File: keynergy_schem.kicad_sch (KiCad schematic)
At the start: 4 parts, among them SW1 SW_DPDT_x2, SW2 SW_DPDT_x2, SW3 SW_DPDT_x2, SW4 SW_DPDT_x2

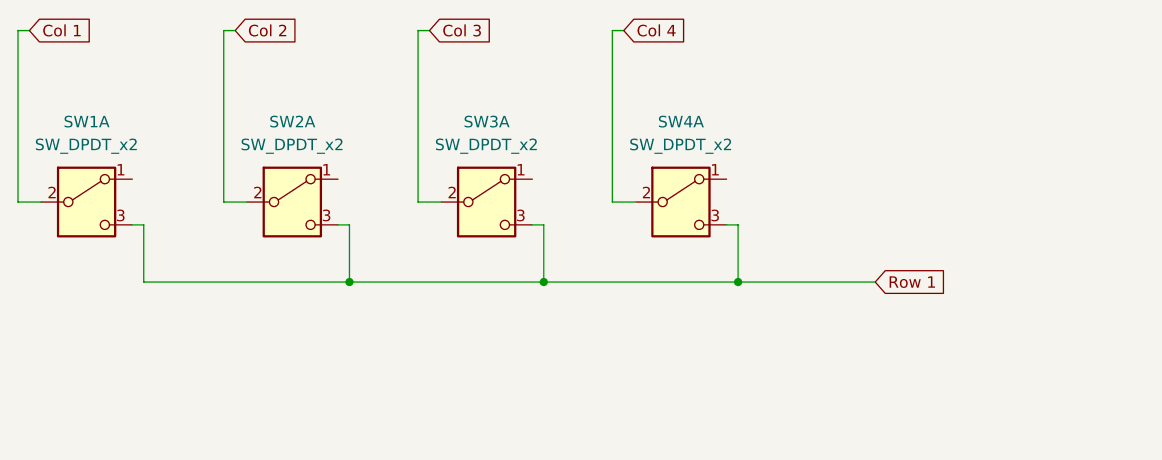
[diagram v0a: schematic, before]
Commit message: custom selonoid key added
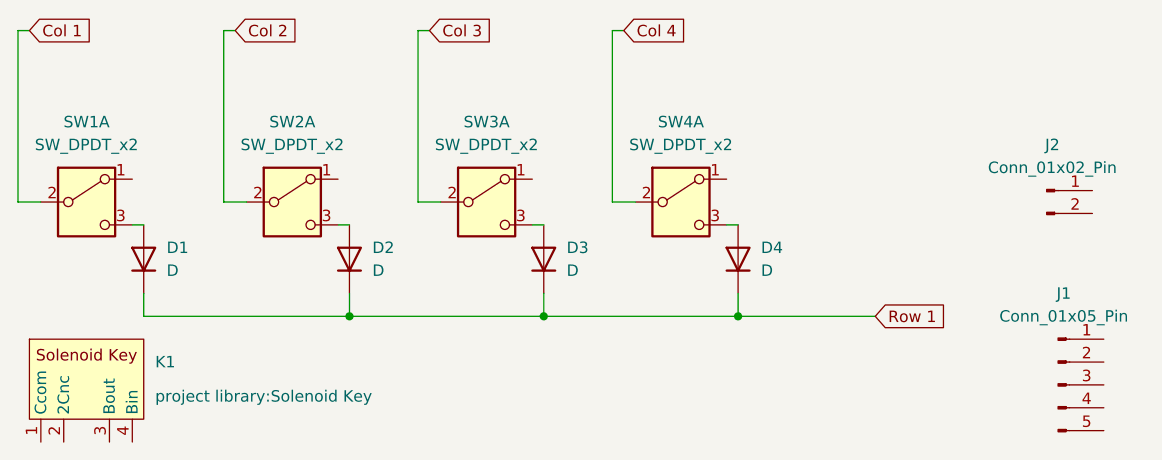
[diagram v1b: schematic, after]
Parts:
- added D1, D2, D3, D4: D, Diode_THT:D_DO-35_SOD27_P7.62mm_Horizontal, symbol Device:D
- added J1: Conn_01x05_Pin, symbol Connector:Conn_01x05_Pin
- added J2: Conn_01x02_Pin, symbol Connector:Conn_01x02_Pin
- added K1: ~, project library:Solenoid Key, symbol Key_symbol:Solenoid_Key
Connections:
- net Row 1: now also D1.1 (K), D2.1 (K), D3.1 (K), D4.1 (K); no longer SW1.3 (C), SW2.3 (C), SW3.3 (C), SW4.3 (C)
- new net: D1.2 (A), SW1.3 (C)
- new net: D3.2 (A), SW3.3 (C)
- new net: D2.2 (A), SW2.3 (C)
- new net: D4.2 (A), SW4.3 (C)

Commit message: new files
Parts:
- removed J1: Conn_01x05_Pin, symbol Connector:Conn_01x05_Pin
- removed J2: Conn_01x02_Pin, symbol Connector:Conn_01x02_Pin
- removed SW1, SW2, SW3, SW4: SW_DPDT_x2, symbol Switch:SW_DPDT_x2
- added J1: Conn_01x03_Pin, Connector_PinHeader_2.54mm:PinHeader_1x03_P2.54mm_Vertical, symbol Connector:Conn_01x03_Pin
- added J3: Conn_01x04_Pin, Connector_PinHeader_2.54mm:PinHeader_1x04_P2.54mm_Vertical, symbol Connector:Conn_01x04_Pin
- added K2, K3, K4: ~, project library:Solenoid Key, symbol Key_symbol:Solenoid_Key
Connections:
- net Col 1: now also K1.4 (Bin), J3.1 (Pin_1)
- net Col 2: now also J3.2 (Pin_2), K2.4 (Bin)
- net Col 3: now also J3.3 (Pin_3), K3.4 (Bin), K4.4 (Bin)
- net Col 4: now also J3.4 (Pin_4)
- net Row 1: now also J1.1 (Pin_1)
- net at D1.2 (A): now also K1.3 (Bout)
- net at D3.2 (A): now also K3.3 (Bout)
- net at D2.2 (A): now also K2.3 (Bout)
- net Row 3: now reaches K1.1 (C1)
- net Row 3: now also J1.3 (Pin_3)
- net at K1.2 (C2): now also K2.1 (C1)
- net at D4.2 (A): now also K4.3 (Bout)
- new net: K2.2 (C2), K3.1 (C1)
- new net: K3.2 (C2), K4.1 (C1)
- new net Row 2: J1.2 (Pin_2), K4.2 (C2)
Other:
- moved on the sheet: D1, D2, D3, D4, K1

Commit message: new files
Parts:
- added D10, D11, D5, D6, D7, D8, D9: D, Diode_THT:D_DO-35_SOD27_P7.62mm_Horizontal, symbol Device:D
- added J2, J6, J8: Conn_01x03_Pin, Connector_PinHeader_2.54mm:PinHeader_1x03_P2.54mm_Vertical, symbol Connector:Conn_01x03_Pin
- added J4, J5, J7: Conn_01x04_Pin, Connector_PinHeader_2.54mm:PinHeader_1x04_P2.54mm_Vertical, symbol Connector:Conn_01x04_Pin
- added K10, K11, K5, K6, K7, K8, K9: ~, project library:Solenoid Key, symbol Key_symbol:Solenoid_Key
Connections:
- net Row 2: now also D5.1 (K), D6.1 (K), D7.1 (K), J2.1 (Pin_1); no longer J1.2 (Pin_2), K4.2 (C2)
- net Col 1 renamed Col 1-1
- net Col 2 renamed Col 1-2
- net Col 3 renamed Col 1-3
- net Col 1-3: no longer K4.4 (Bin)
- net Col 4 renamed Col 1-4
- net Col 1-4: now also K4.4 (Bin)
- net Row 3 renamed Coil 1-2
- new net: D11.2 (A), K11.3 (Bout)
- new net: K6.2 (C2), K7.1 (C1)
- new net: D7.2 (A), K7.3 (Bout)
- new net: D10.2 (A), K10.3 (Bout)
- new net: K5.2 (C2), K6.1 (C1)
- new net: D6.2 (A), K6.3 (Bout)
- new net: D8.2 (A), K8.3 (Bout)
- new net: D5.2 (A), K5.3 (Bout)
- new net: K10.2 (C2), K11.1 (C1)
- new net: D9.2 (A), K9.3 (Bout)
- new net: K8.2 (C2), K9.1 (C1)
- new net Coil 1-1: J1.2 (Pin_2), K4.2 (C2)
- new net Coil 2-1: J2.2 (Pin_2), K7.2 (C2)
- new net Coil 2-2: J2.3 (Pin_3), K5.1 (C1)
- new net Coil 5-1: J6.2 (Pin_2), K9.2 (C2)
- new net Coil 5-2: J6.3 (Pin_3), K8.1 (C1)
- new net Coil 5-3: J8.2 (Pin_2), K11.2 (C2)
- new net Coil 5-4: J8.3 (Pin_3), K10.1 (C1)
- new net Col 2-1: J4.1 (Pin_1), K5.4 (Bin)
- new net Col 2-2: J4.2 (Pin_2), K6.4 (Bin)
- new net Col 2-3: J4.3 (Pin_3), K7.4 (Bin)
- new net Col 2-4: J4.4 (Pin_4)
- new net Col 5: D10.1 (K), D11.1 (K), J8.1 (Pin_1)
- new net Col 5-1: J5.1 (Pin_1), K8.4 (Bin)
- new net Col 5-2: J5.2 (Pin_2), K9.4 (Bin)
- new net Col 5-3: J5.3 (Pin_3)
- new net Col 5-4: J5.4 (Pin_4)
- new net Row 5: D8.1 (K), D9.1 (K), J6.1 (Pin_1)
- new net Row 5-1: J7.1 (Pin_1), K10.4 (Bin)
- new net Row 5-2: J7.2 (Pin_2), K11.4 (Bin)
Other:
- moved on the sheet: D1, D2, D3, D4, J1, J3, K1, K2, K3, K4

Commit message: new
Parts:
- removed J4: Conn_01x04_Pin, Connector_PinHeader_2.54mm:PinHeader_1x04_P2.54mm_Vertical, symbol Connector:Conn_01x04_Pin
- added J4: Conn_01x03_Pin, Connector_PinHeader_2.54mm:PinHeader_1x03_P2.54mm_Vertical, symbol Connector:Conn_01x03_Pin
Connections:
- net Col 2-1: now also J4.1 (Pin_1)
- net Col 2-2: now also J4.2 (Pin_2)
- net Col 2-3: now also J4.3 (Pin_3)
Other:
- note added: "Row 1, Col 1-4"
- note added: "Row 2-4, Col 1-3"
- note added: "Row 2/3 - 4/5, Col 5"
- note added: "Row 5, Col 1-2/3"
- moved on the sheet: J7, J8

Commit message: new update
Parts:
- removed J5, J7: Conn_01x04_Pin, Connector_PinHeader_2.54mm:PinHeader_1x04_P2.54mm_Vertical, symbol Connector:Conn_01x04_Pin
- added J5, J7: Conn_01x02_Pin, Connector_PinHeader_2.54mm:PinHeader_1x02_P2.54mm_Vertical, symbol Connector:Conn_01x02_Pin
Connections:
- net Col 5-1: now also J5.1 (Pin_1)
- net Col 5-2: now also J5.2 (Pin_2)
- net Row 5-1: now also J7.1 (Pin_1)
- net Row 5-2: now also J7.2 (Pin_2)
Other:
- note added: "Row 5, Col 1/2-3"
- note removed: "Row 5, Col 1-2/3"

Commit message: new
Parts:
- added A2: RaspberryPi_Pico_W, Module:RaspberryPi_Pico_Common_THT, symbol MCU_Module:RaspberryPi_Pico_W
- added BT1: Battery_Cell, symbol Device:Battery_Cell
- added C1: 1000uF, Capacitor_THT:CP_Radial_D8.0mm_P5.00mm, symbol Device:C_Polarized
- added D12, D13, D15: D, Diode_THT:D_DO-34_SOD68_P7.62mm_Horizontal, symbol Device:D
- added D14: 1N5819, Diode_THT:D_DO-34_SOD68_P7.62mm_Horizontal, symbol Device:D
- added R1, R2: 10k, Resistor_THT:R_Axial_DIN0204_L3.6mm_D1.6mm_P7.62mm_Horizontal, symbol Device:R_Small
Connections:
- new net: A2.21 (GPIO16), R1.2, R2.1
- new net: A2.13 (GND), A2.18 (GND), A2.23 (GND), A2.28 (GND), A2.3 (GND), A2.38 (GND), A2.8 (GND)
- new net COL1: A2.9 (GPIO6)
- new net COL2: A2.10 (GPIO7)
- new net COL3: A2.11 (GPIO8)
- new net COL4: A2.12 (GPIO9)
- new net Combined Coil 1: D12.2 (A), D13.1 (K)
- new net Combined Coil 2: D14.1 (K), D15.2 (A)
- new net IN+: C1.1, D12.1 (K), D15.1 (K), R1.1
- new net IN-: C1.2, D13.2 (A), D14.2 (A), R2.2
- new net OUT+: BT1.1 (+)
- new net OUT-: BT1.2 (-)
- new net ROW1: A2.4 (GPIO2)
- new net ROW2: A2.5 (GPIO3)
- new net ROW3: A2.6 (GPIO4)
- new net ROW4: A2.7 (GPIO5)
- new net ROW5: A2.14 (GPIO10)
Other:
- moved on the sheet: J1

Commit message: new
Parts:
- removed D1, D10, D11, D2, D3, D4, D5, D6, D7, D8, D9: D, Diode_THT:D_DO-35_SOD27_P7.62mm_Horizontal, symbol Device:D
- removed J2, J4, J6, J8: Conn_01x03_Pin, Connector_PinHeader_2.54mm:PinHeader_1x03_P2.54mm_Vertical, symbol Connector:Conn_01x03_Pin
- removed J5, J7: Conn_01x02_Pin, Connector_PinHeader_2.54mm:PinHeader_1x02_P2.54mm_Vertical, symbol Connector:Conn_01x02_Pin
- added C2: C_Polarized_Small, Capacitor_THT:CP_Radial_D8.0mm_P3.50mm, symbol Device:C_Polarized_Small
- added D1, D2, D3, D4: 1N5818, Diode_THT:D_DO-41_SOD81_P10.16mm_Horizontal, symbol Diode:1N5818
- added K12, K13, K14, K15, K16, K17, K18, K19, K20: ~, project library:Solenoid Key, symbol Key_symbol:Solenoid_Key
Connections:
- net Col 5-2 is gone; now on net Column 1: K9.4 (Bin)
- net Row 5-1 is gone; now on net Column 2: K10.4 (Bin)
- net Row 5-2 is gone; now on net Column 3: K11.4 (Bin)
- net Coil 2-1: now also K8.2 (C2); no longer K7.2 (C2)
- net Coil 5-1: now also K19.2 (C2); no longer K9.2 (C2)
- net Coil 5-2: now also K17.1 (C1); no longer K8.1 (C1)
- net Col 1-1: no longer K1.4 (Bin)
- net Col 1-2: no longer K2.4 (Bin)
- net Col 1-3: no longer K3.4 (Bin)
- net Col 1-4: no longer K4.4 (Bin)
- net Row 1: now also K1.3 (Bout), K2.3 (Bout), K3.3 (Bout), K4.3 (Bout)
- net Row 2: now also K5.3 (Bout), K6.3 (Bout), K7.3 (Bout), K8.3 (Bout)
- net Row 5: now also K17.3 (Bout), K18.3 (Bout), K19.3 (Bout), K20.3 (Bout)
- net Row 3: now reaches K11.3 (Bout)
- net Row 3: now also K10.3 (Bout), K9.3 (Bout), K12.3 (Bout)
- net Coil 3-2: now reaches K9.1 (C1)
- net Coil 3-2: no longer K8.2 (C2)
- net Coil 5-3 renamed Coil 3-1
- net Coil 5-4: no longer names the net of K10.1 (C1)
- net Coil 5-4: now also K9.2 (C2)
- net Col 2-1 renamed Column 1
- net Column 1: now also K1.4 (Bin), K13.4 (Bin), K17.4 (Bin)
- net Col 2-2 renamed Column 2
- net Column 2: now also K2.4 (Bin), K14.4 (Bin), K18.4 (Bin)
- net Col 2-3 renamed Column 3
- net Column 3: now also K3.4 (Bin), K15.4 (Bin), K19.4 (Bin)
- net Col 5-1 renamed Column 4
- net Column 4: now also K4.4 (Bin), K12.4 (Bin), K16.4 (Bin), K20.4 (Bin)
- new net: K17.2 (C2), K18.1 (C1)
- new net: K7.2 (C2), K8.1 (C1)
- new net: C2.2, D3.1 (K), D4.2 (A)
- new net: D1.2 (A), D3.2 (A)
- new net: K13.2 (C2), K14.1 (C1)
- new net: K14.2 (C2), K15.1 (C1)
- new net: C2.1, D2.1 (K), D4.1 (K)
- new net: D1.1 (K), D2.2 (A)
- new net: K18.2 (C2), K19.1 (C1)
- new net Coil 4-1: K15.2 (C2)
- new net Coil 4-2: K13.1 (C1)
- new net Row 4: K13.3 (Bout), K14.3 (Bout), K15.3 (Bout), K16.3 (Bout)
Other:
- note removed: "Row 1, Col 1-4"
- note removed: "Row 2-4, Col 1-3"
- note removed: "Row 2/3 - 4/5, Col 5"
- note removed: "Row 5, Col 1/2-3"
- moved on the sheet: A2, BT1, C1, D12, D13, D14, D15, J1, J3, K10, K11, K5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

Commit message: new update
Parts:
- removed J1: Conn_01x03_Pin, Connector_PinHeader_2.54mm:PinHeader_1x03_P2.54mm_Vertical, symbol Connector:Conn_01x03_Pin
- added J2, J4, J5, J6: Conn_01x04_Pin, Connector_PinHeader_2.54mm:PinHeader_1x04_P2.54mm_Vertical, symbol Connector:Conn_01x04_Pin
- added J3: Conn_01x02_Pin, Connector_PinHeader_2.54mm:PinHeader_1x02_P2.54mm_Vertical, symbol Connector:Conn_01x02_Pin
- D1, D2, D3, D4: footprint Diode_THT:D_DO-41_SOD81_P10.16mm_Horizontal -> Diode_THT:D_DO-34_SOD68_P7.62mm_Horizontal
- renumbered J3 to J1
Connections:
- net Col 1-1 is gone; now on net Column 1: J1.1 (Pin_1)
- net Col 1-2 is gone; now on net Column 2: J1.2 (Pin_2)
- net Col 1-3 is gone; now on net Column 3: J1.3 (Pin_3)
- net Col 1-4 is gone; now on net Column 4: J1.4 (Pin_4)
- net Coil 1-1: now also J4.2 (Pin_2)
- net Coil 1-2: now also J4.1 (Pin_1)
- net Coil 2-1: now also J4.4 (Pin_4)
- net Coil 2-2: now also J4.3 (Pin_3)
- net Column 1: now also J2.1 (Pin_1), J5.1 (Pin_1), J6.1 (Pin_1)
- net Column 2: now also J2.2 (Pin_2), J5.2 (Pin_2), J6.2 (Pin_2)
- net Column 3: now also J2.3 (Pin_3), J5.3 (Pin_3), J6.3 (Pin_3)
- net Column 4: now also J2.4 (Pin_4), J5.4 (Pin_4), J6.4 (Pin_4)
- net Row 1: now also J3.1 (Pin_1)
- net Row 2: now also J3.2 (Pin_2)
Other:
- note added: "COIL TO PARALLEL"
- note added: "OUT to MCU"
- note added: "PCB 1"
- moved on the sheet: J1, K1, K10, K11, K12, K13, K14, K15, K16, K17, K18, K19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
